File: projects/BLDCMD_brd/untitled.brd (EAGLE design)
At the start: 80 x 50 mm, 92 parts, among them IC1 STM32F103C8, IC10 7805DT, IC12 BSS138BK, IC3 NCV7351D1E, IC4 74AHCT1G08DCK, IC5 74AHCT1G08DCK, IC6 74AHCT1G08DCK, IC7 SI8621AB-B-IS, IC8 7815DT, IC9 MC34063AD, Q1 N-MOSFET-, Q2 N-MOSFET-, Q3 N-MOSFET-, Q4 N-MOSFET-, Q5 N-MOSFET-, Q6 N-MOSFET-, X1 8P8C-LED

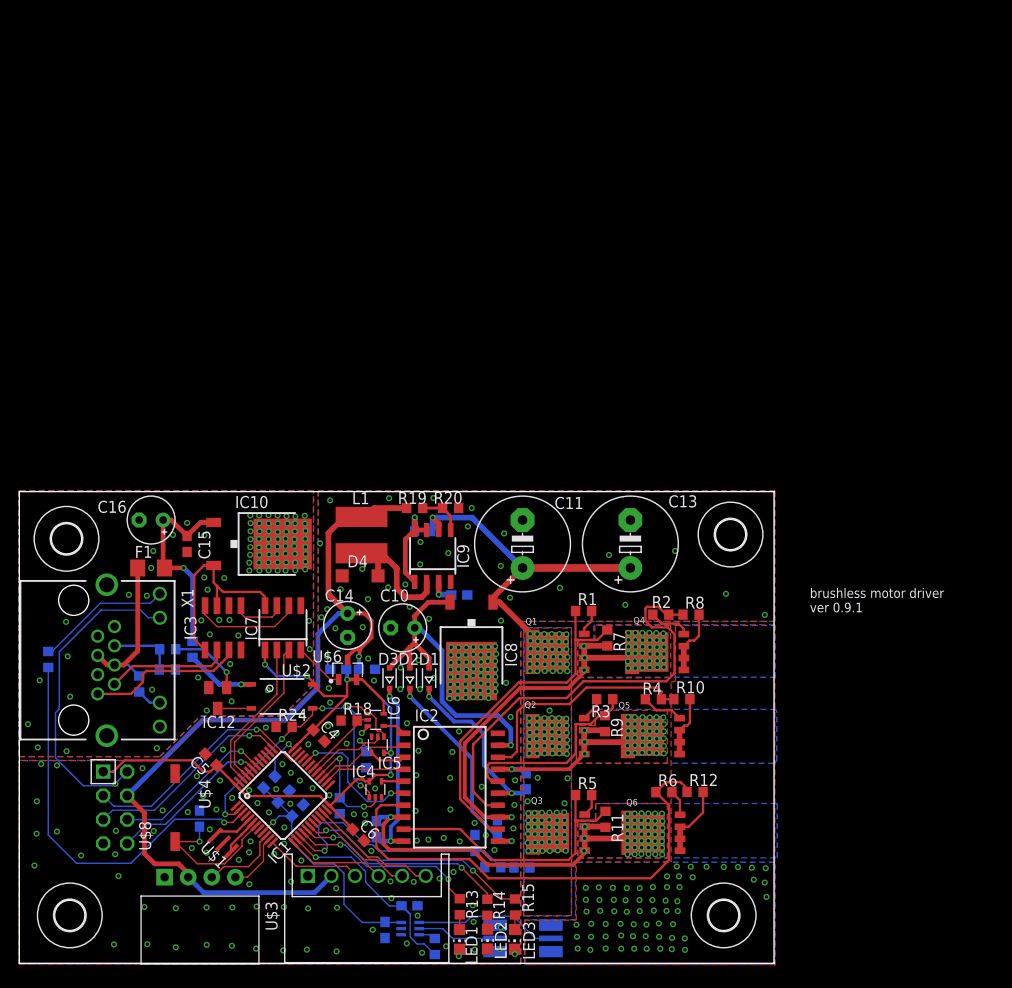
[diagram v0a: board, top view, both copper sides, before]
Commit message: usbcan 修正済み　BLDCMD完成
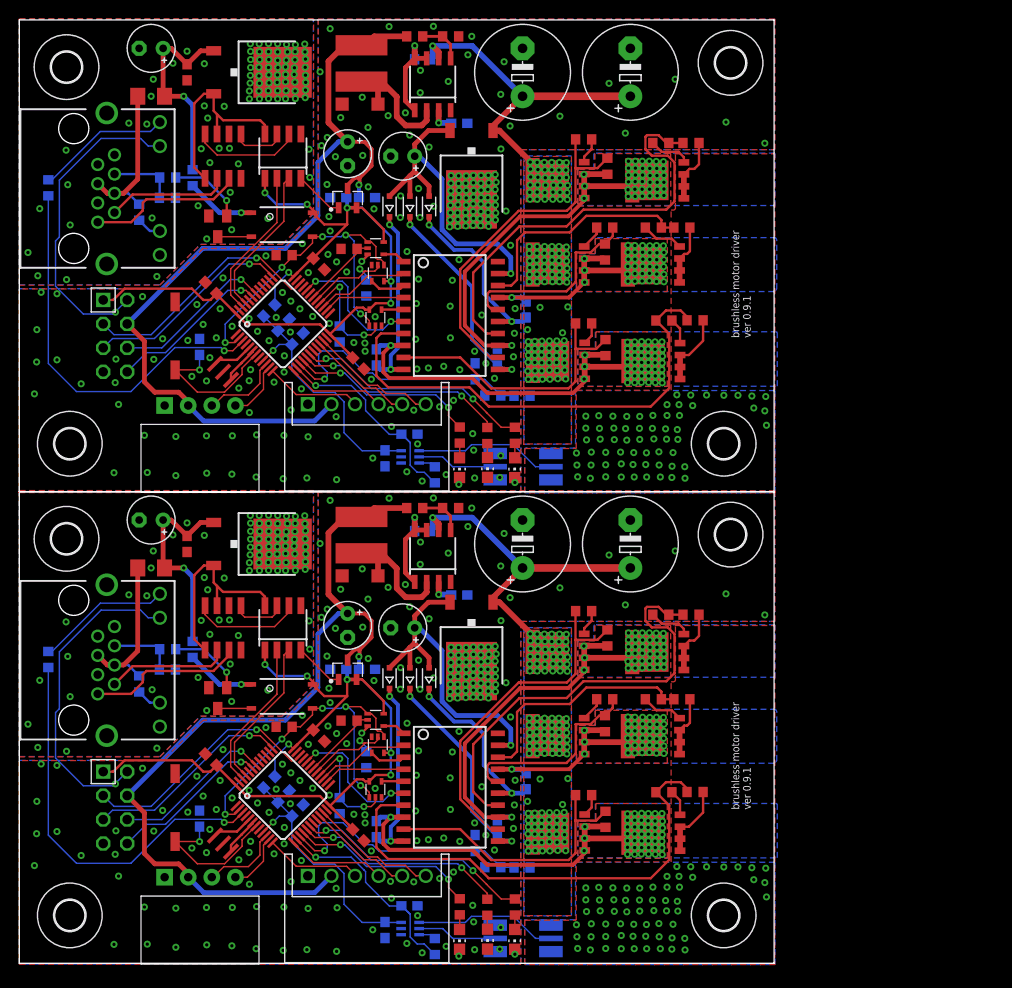
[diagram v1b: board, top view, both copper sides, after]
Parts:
- added B2: FERRITE_BEAD, mylib:R0603
- added C22, C23, C24, C38, C39, C40: (no value), rcl:C0603
- added C25, C26, C27, C28: 100n, rcl:C0603
- added C29: (no value), mylib:C0603
- added C30, C31, C36: 100n, mylib:C0603
- added C32, C33: (no value), rcl:E5-10,5
- added C34, C35, C37: (no value), rcl:E2,5-5
- added C41: 10u, rcl:C0603
- added C42: 1u, rcl:C0603
- added CN2: (no value), jst-xh:S6B-XH-A
- added D5, D6, D7: (no value), diode:SOD323-R
- added D8: (no value), mylib:SOD123
- added F2: (no value), mylib:R1206
- added H5, H6, H7, H8: MOUNT-HOLE3.2, holes:3,2
- added IC11: STM32F103C8, stm32_mcu:LQFP48
- added IC13: (no value), mylib:SOIC20S
- added IC14: NCV7351D1E, on-semi:SO08
- added IC15: SI8621AB-B-IS, mylib:SO08
- added IC16: 7815DT, mylib:TO252
- added IC17: 7805DT, mylib:TO252
- added IC18: MC34063AD, mylib:SOIC8
- added IC19: BSS138BK, mylib:SOT23
- added IC20, IC21, IC22: 74AHCT1G08DCK, mylib:SC70-5
- added L2: L5852, mylib:L5852
- added LED4, LED5, LED6: (no value), mylib:CHIP-LED0805
- added Q10, Q11, Q12, Q7, Q8, Q9: N-MOSFET-, mylib:SOT669
- added R32, R39, R40, R41, R42, R43, R60, R61, R62: 10, mylib:R0603
- added R33, R34, R35, R44, R45, R46: 10k, mylib:R0603
- added R36, R37, R38, R47, R48, R49, R53, R55: 1k, mylib:R0603
- added R50, R51, R52: (no value), mylib:R0603
- added R54: 100k, mylib:R0603
- added R56: 1k?, mylib:R0603
- added R57: 4k7, mylib:R0603
- added R58: 470, mylib:R0603
- added R59: CSS2H-2512, mylib:CSS2H-2512
- added U$10: XH-4-SIDE, con-xh:CON-XH-4-SIDE
- added U$11: SWITCH_TACTILETOP, switch-tactile:SWITCH_TACTILE_3X6
- added U$12: XC6206, torex:SOT95P240X110-3
- added U$13: MA04-2, mylib:MA04-2W
- added U$14: NCS199, mylib:SOT65P210X110-6
- added U$7: CSTCE8M00G55, resonator:CSTCE8M00G55
- added U$9: TLP184, mylib:11-4M1S
- added X2: 8P8C-LED, mylib:8P8C-LED
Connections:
- new net !EMS1: IC11.2, IC20.1, IC21.1, IC22.1, R55.2, U$9.3
- new net !RESET1: C28.1, IC11.7, U$11.P$2
- new net +15V1: C35.+, D5.A, D6.A, D7.A, IC13.19, IC16.2
- new net +3V1: B2.2, C25.1, C26.1, C27.1, C31.1, IC11.24, IC11.36, IC11.48, IC15.1, IC20.5, IC21.5, IC22.5, U$12.2, U$13.8, U$9.4
- new net +5V1: C30.1, C34.+, CN2.2, L2.P$2, R50.2, U$10.P$2, U$12.3, U$13.5
- new net 24V_ISO1: C36.1, C37.+, F2.1, IC17.1, R56.2
- new net 3V3A1: B2.1, C39.1, C41.1, C42.1, IC11.9, U$14.3
- new net 5V_ISO1: IC14.3, IC14.5, IC15.8, IC17.2
- new net CANRX1: IC11.45, IC15.3
- new net CANTX1: IC11.46, IC15.2
- new net ENC_A1: IC11.10, U$10.P$3
- new net ENC_B1: IC11.11, U$10.P$4
- new net GNDA1: C25.2, C26.2, C27.2, C28.2, C29.2, C30.2, C31.2, C32.-, C33.-, C34.-, C35.-, C38.2, C39.2, C40.2, C41.2, C42.2, CN2.1, D8.A, IC11.23, IC11.35, IC11.44, IC11.47, IC11.8, IC13.20, IC15.4, IC16.3, IC18.4, IC20.3, IC21.3, IC22.3, LED4.C, LED5.C, LED6.C, R47.1, R48.1, R49.1, R51.1, R55.1, R59.1$1, R59.1$2, R62.1, U$10.P$1, U$11.P$1, U$12.1, U$13.2, U$13.7, U$14.1, U$14.2, U$7.2, X2.YC
- new net GNDIO1: C36.2, C37.-, IC14.2, IC14.8, IC15.5, IC17.3, IC19.2, R54.1, X2.3, X2.7, X2.8, X2.GC, X2.M1, X2.M2
- new net HIN4: IC13.5, IC20.4
- new net HIN5: IC13.3, IC21.4
- new net HIN6: IC13.1, IC22.4
- new net HO4: IC13.12, R32.1, R44.1
- new net HO5: IC13.16, R40.1, R46.1
- new net HO6: IC13.9, R34.1, R42.1
- new net IN_A1: CN2.3, IC11.12
- new net IN_B1: CN2.4, IC11.13
- new net IN_C1: CN2.5, IC11.21
- new net IN_D1: CN2.6, IC11.22
- new net ISENSE1: C38.1, IC11.14, R60.2
- new net LED3: IC11.16, R36.1
- new net LED4: IC11.17, R37.1
- new net LED5: IC11.18, R38.1
- new net LED_CAN1: IC11.3, R58.2
- new net LIN4: IC11.27, IC13.2
- new net LIN5: IC11.32, IC13.6
- new net LIN6: IC11.26, IC13.4
- new net LO4: IC13.14, R39.1, R45.1
- new net LO5: IC13.18, R33.1, R41.1
- new net LO6: IC13.7, R35.1, R43.1
- new net N$34: IC11.6, U$7.3
- new net N$35: IC11.5, U$7.1
- new net N$39: IC11.28, IC20.2, R47.2
- new net N$40: LED6.A, R38.2
- new net N$41: LED4.A, R36.2
- new net N$42: LED5.A, R37.2
- new net N$43: Q7.4, R32.2
- new net N$44: Q10.4, R39.2
- new net N$45: Q8.4, R40.2
- new net N$46: Q11.4, R41.2
- new net N$47: Q9.4, R42.2
- new net N$48: Q12.4, R43.2
- new net N$49: C22.1, D5.C, IC13.15
- new net N$50: C23.1, D6.C, IC13.11
- new net N$51: C24.2, D7.C, IC13.10
- new net N$52: IC14.7, X2.1
- new net N$53: IC14.6, X2.2
- new net N$54: IC11.29, IC21.2, R48.2
- new net N$55: IC11.30, IC22.2, R49.2
- new net N$56: IC14.1, IC15.7
- new net N$57: IC14.4, IC15.6
- new net N$58: R53.2, R54.2, X2.6
- new net N$59: F2.2, R57.2, X2.4, X2.5
- new net N$60: D8.C, IC18.2, L2.P$1
- new net N$61: IC18.5, R50.1, R51.2
- new net N$62: IC18.1, IC18.7, IC18.8, R52.1
- new net N$63: C29.1, IC18.3
- new net N$64: IC19.1, R53.1
- new net N$65: IC19.3, U$9.2
- new net N$66: R56.1, U$9.1
- new net N$67: R57.1, X2.GA
- new net N$68: R58.1, X2.YA
- new net N$69: Q10.1, Q10.2, Q10.3, Q11.1, Q11.2, Q11.3, Q12.1, Q12.2, Q12.3, R33.2, R35.2, R45.2, R59.2$1, R59.2$2
- new net N$70: R59.2S, U$14.4
- new net N$71: R59.1S, U$14.5
- new net N$72: R60.1, U$14.6
- new net SWCLK1: IC11.37, U$13.4
- new net SWDIO1: IC11.34, U$13.6
- new net U1: C23.2, IC13.13, Q10.5, Q7.1, Q7.2, Q7.3, R44.2
- new net UART_RX1: IC11.43, U$13.1
- new net UART_TX1: IC11.42, U$13.3
- new net V1: C22.2, IC13.17, Q11.5, Q8.1, Q8.2, Q8.3, R46.2
- new net VCC1: C32.+, C33.+, IC16.1, IC18.6, Q7.5, Q8.5, Q9.5, R52.2, R61.2
- new net VSENSE1: C40.1, IC11.15, R61.1, R62.2
- new net W1: C24.1, IC13.8, Q12.5, Q9.1, Q9.2, Q9.3, R34.2
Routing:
- net +5V1: track 0.00 -> 93.4 mm, vias 0 -> 1
- net +3V1: track 0.00 -> 86.1 mm, vias 0 -> 6
- net LO6: track 0.00 -> 52.4 mm
- net LO4: track 0.00 -> 46.2 mm
- net LED_CAN1: track 0.00 -> 42.1 mm, vias 0 -> 1
- net U1: track 0.00 -> 42.0 mm, vias 0 -> 40
- net W1: track 0.00 -> 40.7 mm, vias 0 -> 46
- net GNDA1: track 0.00 -> 40.0 mm, vias 0 -> 206
- net VCC1: track 0.00 -> 39.3 mm, vias 0 -> 113
- net !EMS1: track 0.00 -> 38.0 mm, vias 0 -> 5
- net +15V1: track 0.00 -> 37.3 mm, vias 0 -> 1
- net HO4: track 0.00 -> 37.1 mm
- net HO6: track 0.00 -> 29.6 mm
- net VSENSE1: track 0.00 -> 29.2 mm, vias 0 -> 1
- net 3V3A1: track 0.00 -> 27.9 mm, vias 0 -> 1
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- added copper zone on layer 1, net GNDA1
- added copper zone on layer 16, net GNDA1
- added copper zone on layer 1, net GNDIO1
- added copper zone on layer 16, net GNDIO1
- added copper zone on layer 1, net N$69
- added copper zone on layer 16, net N$69
- added copper zone on layer 1, net U1
- added copper zone on layer 16, net U1
- added copper zone on layer 1, net V1
- added copper zone on layer 16, net V1
- added copper zone on layer 1, net VCC1
- added copper zone on layer 16, net VCC1
- added copper zone on layer 1, net W1
- added copper zone on layer 16, net W1
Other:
- board size 80 x 50 mm -> 80 x 100 mm
- board text added: "B1"
- board text added: "C1"
- board text added: "C10"
- board text added: "C11"
- board text added: "C12"
- board text added: "C13"
- board text added: "C14"
- board text added: "C15"
- board text added: "C16"
- board text added: "C17"
- board text added: "C18"
- board text added: "C19"
- board text added: "C2"
- board text added: "C20"
- board text added: "C21"
- board text added: "C3"
- board text added: "C4"
- board text added: "C5"
- board text added: "C6"
- board text added: "C7"
- board text added: "C8"
- board text added: "C9"
- board text added: "D1"
- board text added: "D2"
- board text added: "D3"
- board text added: "D4"
- board text added: "F1"
- board text added: "IC1"
- board text added: "IC10"
- board text added: "IC12"
- board text added: "IC2"
- board text added: "IC3"
- board text added: "IC4"
- board text added: "IC5"
- board text added: "IC6"
- board text added: "IC7"
- board text added: "IC8"
- board text added: "IC9"
- board text added: "L1"
- board text added: "LED1"
- board text added: "LED2"
- board text added: "LED3"
- board text added: "Q1"
- board text added: "Q2"
- board text added: "Q3"
- board text added: "Q4"
- board text added: "Q5"
- board text added: "Q6"
- board text added: "R1"
- board text added: "R10"
- board text added: "R11"
- board text added: "R12"
- board text added: "R13"
- board text added: "R14"
- board text added: "R15"
- board text added: "R16"
- board text added: "R17"
- board text added: "R18"
- board text added: "R19"
- board text added: "R2"
- board text added: "R20"
- board text added: "R21"
- board text added: "R22"
- board text added: "R23"
- board text added: "R24"
- board text added: "R25"
- board text added: "R26"
- board text added: "R27"
- board text added: "R28"
- board text added: "R29"
- board text added: "R3"
- board text added: "R30"
- board text added: "R31"
- board text added: "R4"
- board text added: "R5"
- board text added: "R6"
- board text added: "R7"
- board text added: "R8"
- board text added: "R9"
- board text added: "U$1"
- board text added: "U$2"
- board text added: "U$4"
- board text added: "U$5"
- board text added: "U$6"
